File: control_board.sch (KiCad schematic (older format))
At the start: 18 parts, among them IC1 ATMEGA328P-A, J1 USB_C_Receptacle, J2 AVR-ISP-6, P1 CONN_8, U1 MCP7940N-xSN, Y1 Crystal_GND23

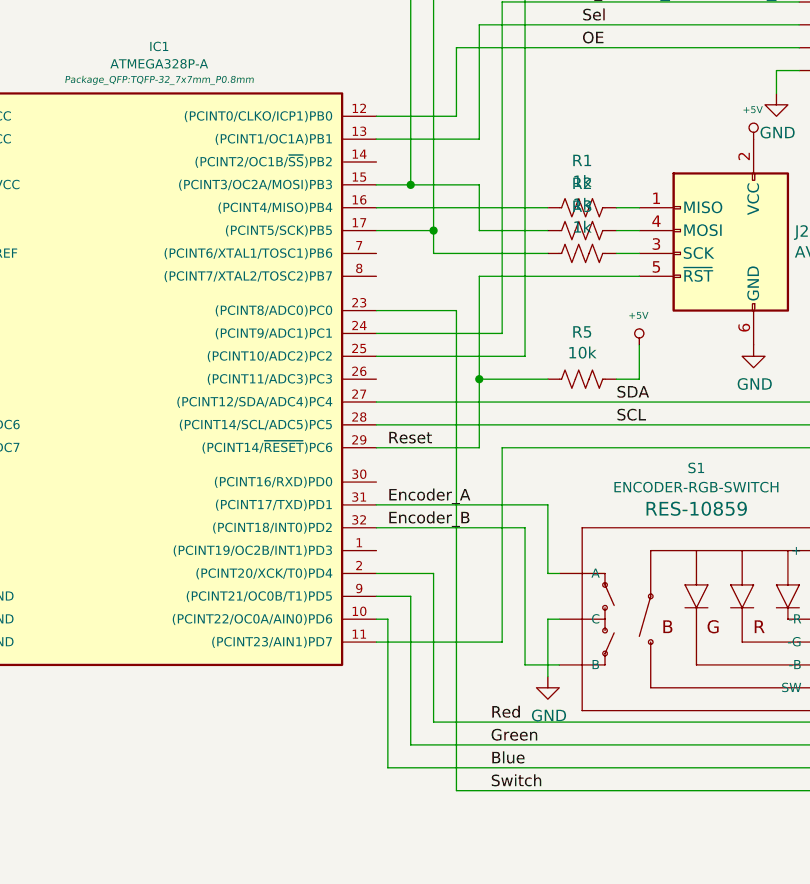
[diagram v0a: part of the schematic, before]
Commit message: Update for board rev 2
Move USB connector to board edge
Move resisters to not interfere with programming header
Widen board to fit enclosure
Move programming header and USB connector away from top/bottom of board for more clearance with enclosure
Move red encoder LED to a PWM capable pin
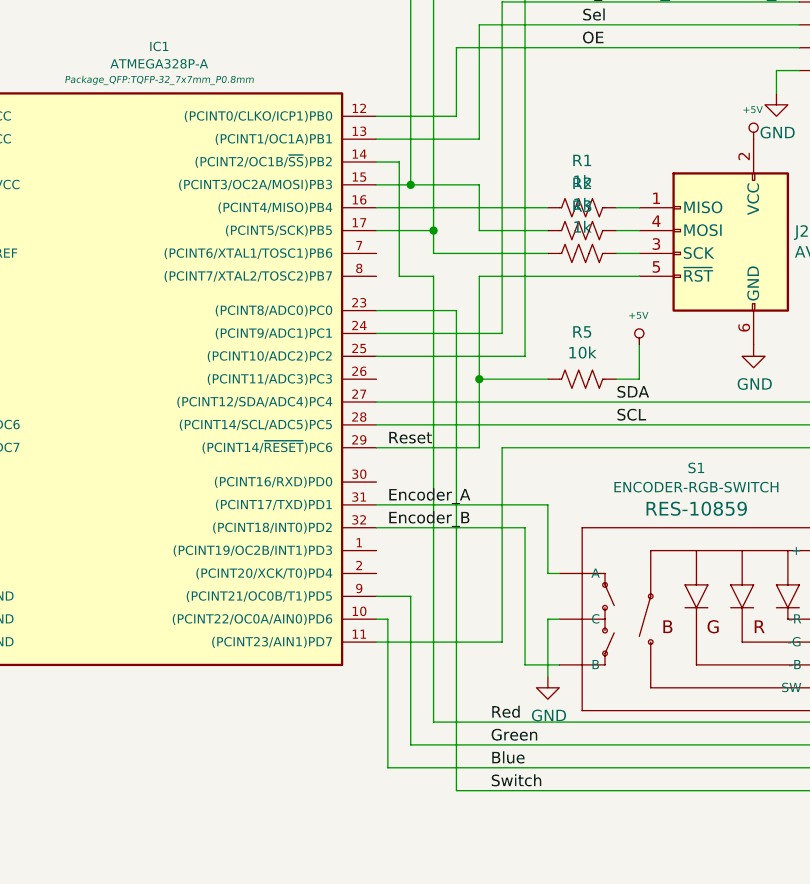
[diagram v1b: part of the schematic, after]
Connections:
- net Red: now also IC1.14 ((PCINT2/OC1B/~SS~)PB2); no longer IC1.2 ((PCINT20/XCK/T0)PD4)
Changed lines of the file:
@@
 	5250 5800 7250 5800
-Wire Wire Line
-	4900 4850 5150 4850
-Wire Wire Line
-	5150 4850 5150 5500
 Wire Wire Line
 	5150 5500 6950 5500
@@
 Wire Wire Line
 	5350 3550 6050 3550
+Wire Wire Line
+	5150 3550 5000 3550
+Wire Wire Line
+	5000 3550 5000 3050
+Wire Wire Line
+	5000 3050 4900 3050
+Wire Wire Line
+	5150 3550 5150 5500
 $EndSCHEMATC
